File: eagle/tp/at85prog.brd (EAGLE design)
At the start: 39 x 17.8 mm, 6 parts, among them J1 ICSP, U1 TINY45-20-DIP

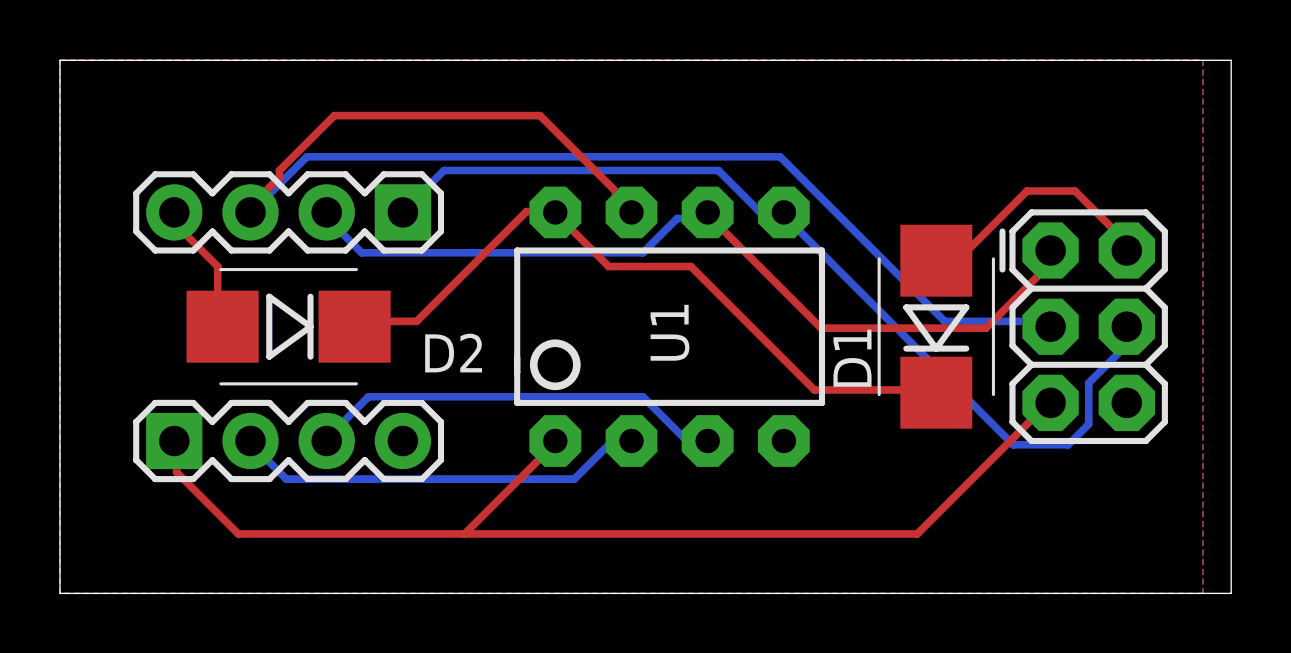
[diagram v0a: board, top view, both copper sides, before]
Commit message: tp: add reset button.
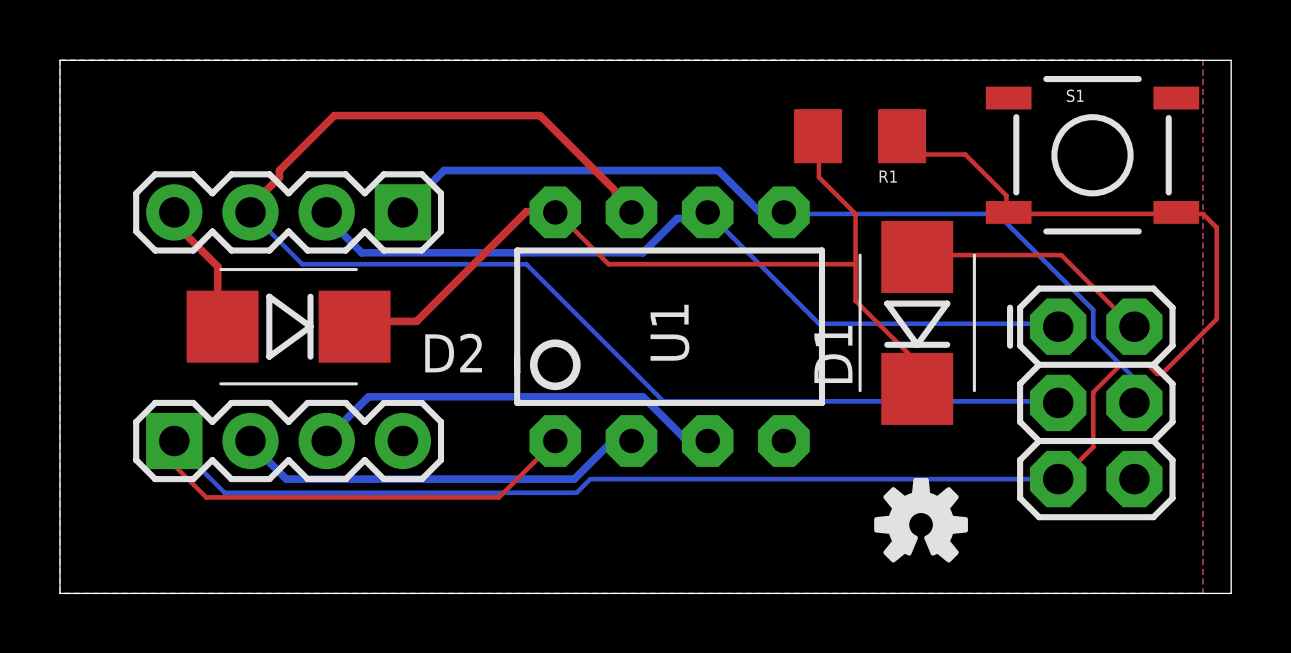
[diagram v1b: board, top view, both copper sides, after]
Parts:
- added LOGO1: OSHW-LOGOS, SparkFun-Aesthetics:OSHW-LOGO-S
- added R1: 10k, SparkFun-Passives:1206
- added S1: Tactile Switches, gipi:TACTILE-SWITCH-SMD
- moved J1 2.55 mm to (33.3, 73.7)
- moved D1 0.65 mm to (28.6, 73.8)
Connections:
- net GND: now also S1.1, S1.2
- net N$4: now also R1.1, S1.3, S1.4
- net VCC: now also R1.2
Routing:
- net N$4: track 37.2 -> 69.1 mm
- net VCC: track 23.6 -> 28.9 mm
- net N$1: track 31.4 -> 29.2 mm
- net N$2: track 28.3 -> 27.2 mm
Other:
- board text removed: "TODO ---- 1. add reset button"
